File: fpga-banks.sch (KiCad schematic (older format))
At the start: 14 parts, among them U1 XC7K70T-FBG484, U2 ASEM1-100.000MHZ-LC-T

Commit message: Update caps around ADC
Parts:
- removed C2, C4: C_1n_0603, lpddr4-test-board-footprints:0603-cap, symbol lpddr4-test-board:C_1n_0603
- added C2, C4, C71: C_910p_0402, lpddr4-test-board-footprints:0402-res, symbol lpddr4-test-board:C_910p_0402
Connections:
- wire segments 207 -> 209
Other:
- moved on the sheet: C1
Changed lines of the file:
@@
 Wire Wire Line
 	8150 8700 9025 8700
-Wire Wire Line
-	9325 8700 9650 8700
 $Comp
 L lpddr4-test-board:R_100R_0402 R5
@@
 Wire Wire Line
 	8150 9000 9025 9000
-Wire Wire Line
-	9325 9000 9650 9000
 $Comp
 L lpddr4-test-board:R_100R_0402 R3
@@
 L lpddr4-test-board:C_910p_0402 C1
 U 1 1 6045F2AB
-P 9650 8850
-F 0 "C1" H 9675 8950 60  0000 L CNN
-F 1 "C_910p_0402" H 9650 8700 60  0001 C CNN
-F 2 "lpddr4-test-board-footprints:0402-res" H 9850 9050 60  0001 L CNN
-F 3 "" H 9650 8850 50  0001 C CNN
-F 4 "KEMET" H 9850 9250 60  0001 L CNN "Manufacturer"
-F 5 "C0402C911J5GACTU" H 9850 9150 60  0001 L CNN "MPN"
-F 6 "910p" H 9675 8750 50  0000 L CNN "Val"
-	1    9650 8850
-	1    0    0    -1
-$EndComp
-Wire Wire Line
-	9325 9250 9675 9250
-Wire Wire Line
-	9325 9550 9675 9550
-Wire Wire Line
-	9325 10300 9675 10300
-Wire Wire Line
-	9325 10600 9675 10600
-$Comp
-L lpddr4-test-board:C_1n_0603 C4
-U 1 1 604796AE
-P 9675 10450
-F 0 "C4" H 9700 10550 60  0000 L CNN
-F 1 "C_1n_0603" H 9675 10300 60  0001 C CNN
-F 2 "lpddr4-test-board-footprints:0603-cap" H 9875 10650 60  0001 L CNN
-F 3 "" H 9675 10450 50  0001 C CNN
-F 4 "AVX" H 9875 10850 60  0001 L CNN "Manufacturer"
-F 5 "06031C102JAT2A" H 9875 10750 60  0001 L CNN "MPN"
-F 6 "1n" H 9700 10350 50  0000 L CNN "Val"
-	1    9675 10450
-	1    0    0    -1
-$EndComp
-Connection ~ 9675 10300
-Wire Wire Line
-	9675 10300 10200 10300
-Connection ~ 9675 10600
-Wire Wire Line
-	9675 10600 10200 10600
-$Comp
-L lpddr4-test-board:C_1n_0603 C2
-U 1 1 6049AB42
-P 9675 9400
-F 0 "C2" H 9700 9500 60  0000 L CNN
-F 1 "C_1n_0603" H 9675 9250 60  0001 C CNN
-F 2 "lpddr4-test-board-footprints:0603-cap" H 9875 9600 60  0001 L CNN
-F 3 "" H 9675 9400 50  0001 C CNN
-F 4 "AVX" H 9875 9800 60  0001 L CNN "Manufacturer"
-F 5 "06031C102JAT2A" H 9875 9700 60  0001 L CNN "MPN"
-F 6 "1n" H 9700 9300 50  0000 L CNN "Val"
-	1    9675 9400
-	1    0    0    -1
-$EndComp
-Connection ~ 9675 9250
-Wire Wire Line
-	9675 9250 10200 9250
-Connection ~ 9675 9550
-Wire Wire Line
-	9675 9550 10200 9550
-Connection ~ 9650 8700
-Wire Wire Line
-	9650 8700 10200 8700
-Connection ~ 9650 9000
-Wire Wire Line
-	9650 9000 10200 9000
+P 9700 8850
+F 0 "C1" H 9725 8950 60  0000 L CNN
+F 1 "C_910p_0402" H 9700 8700 60  0001 C CNN
+F 2 "lpddr4-test-board-footprints:0402-res" H 9900 9050 60  0001 L CNN
+F 3 "" H 9700 8850 50  0001 C CNN
+F 4 "KEMET" H 9900 9250 60  0001 L CNN "Manufacturer"
+F 5 "C0402C911J5GACTU" H 9900 9150 60  0001 L CNN "MPN"
+F 6 "910p" H 9725 8750 50  0000 L CNN "Val"
+	1    9700 8850
+	1    0    0    -1
+$EndComp
 Text GLabel 5150 7000 2    50   Input ~ 0
 TMDS_CLK_P
@@
 Connection ~ 8225 1350
 Wire Wire Line
-	9325 9750 10200 9750
-Wire Wire Line
-	9325 10050 10200 10050
+	9325 9750 9700 9750
+Wire Wire Line
+	9325 10050 9700 10050
 Text GLabel 7075 7750 0    50   Input ~ 0
 ETH_REF_CLK
@@
 Text GLabel 10525 4075 2    50   Input ~ 0
 USR_BTN4
+$Comp
+L lpddr4-test-board:C_910p_0402 C4
+U 1 1 5FC5316D
+P 9700 9900
+F 0 "C4" H 9725 10000 60  0000 L CNN
+F 1 "C_910p_0402" H 9700 9750 60  0001 C CNN
+F 2 "lpddr4-test-board-footprints:0402-res" H 9900 10100 60  0001 L CNN
+F 3 "" H 9700 9900 50  0001 C CNN
+F 4 "KEMET" H 9900 10300 60  0001 L CNN "Manufacturer"
+F 5 "C0402C911J5GACTU" H 9900 10200 60  0001 L CNN "MPN"
+F 6 "910p" H 9725 9800 50  0000 L CNN "Val"
+	1    9700 9900
+	1    0    0    -1
+$EndComp
+Connection ~ 9700 9750
+Wire Wire Line
+	9700 9750 10200 9750
+Connection ~ 9700 10050
+Wire Wire Line
+	9700 10050 10200 10050
+Wire Wire Line
+	9325 9250 9700 9250
+Wire Wire Line
+	9325 9550 9700 9550
+Wire Wire Line
+	9325 10300 9700 10300
+Wire Wire Line
+	9325 10600 9700 10600
+$Comp
+L lpddr4-test-board:C_910p_0402 C71
+U 1 1 5FC539B0
+P 9700 10450
+F 0 "C71" H 9725 10550 60  0000 L CNN
+F 1 "C_910p_0402" H 9700 10300 60  0001 C CNN
+F 2 "lpddr4-test-board-footprints:0402-res" H 9900 10650 60  0001 L CNN
+F 3 "" H 9700 10450 50  0001 C CNN
+F 4 "KEMET" H 9900 10850 60  0001 L CNN "Manufacturer"
+F 5 "C0402C911J5GACTU" H 9900 10750 60  0001 L CNN "MPN"
+F 6 "910p" H 9725 10350 50  0000 L CNN "Val"
+	1    9700 10450
+	1    0    0    -1
+$EndComp
+Connection ~ 9700 10300
+Wire Wire Line
+	9700 10300 10200 10300
+Connection ~ 9700 10600
+Wire Wire Line
+	9700 10600 10200 10600
+$Comp
+L lpddr4-test-board:C_910p_0402 C2
+U 1 1 5FC53CE5
+P 9700 9400
+F 0 "C2" H 9725 9500 60  0000 L CNN
+F 1 "C_910p_0402" H 9700 9250 60  0001 C CNN
+F 2 "lpddr4-test-board-footprints:0402-res" H 9900 9600 60  0001 L CNN
+F 3 "" H 9700 9400 50  0001 C CNN
+F 4 "KEMET" H 9900 9800 60  0001 L CNN "Manufacturer"
+F 5 "C0402C911J5GACTU" H 9900 9700 60  0001 L CNN "MPN"
+F 6 "910p" H 9725 9300 50  0000 L CNN "Val"
+	1    9700 9400
+	1    0    0    -1
+$EndComp
+Connection ~ 9700 9250
+Wire Wire Line
+	9700 9250 10200 9250
+Connection ~ 9700 9550
+Wire Wire Line
+	9700 9550 10200 9550
+Connection ~ 9700 8700
+Wire Wire Line
+	9700 8700 10200 8700
+Connection ~ 9700 9000
+Wire Wire Line
+	9700 9000 10200 9000
+Wire Wire Line
+	9325 9000 9700 9000
+Wire Wire Line
+	9325 8700 9700 8700
 $EndSCHEMATC

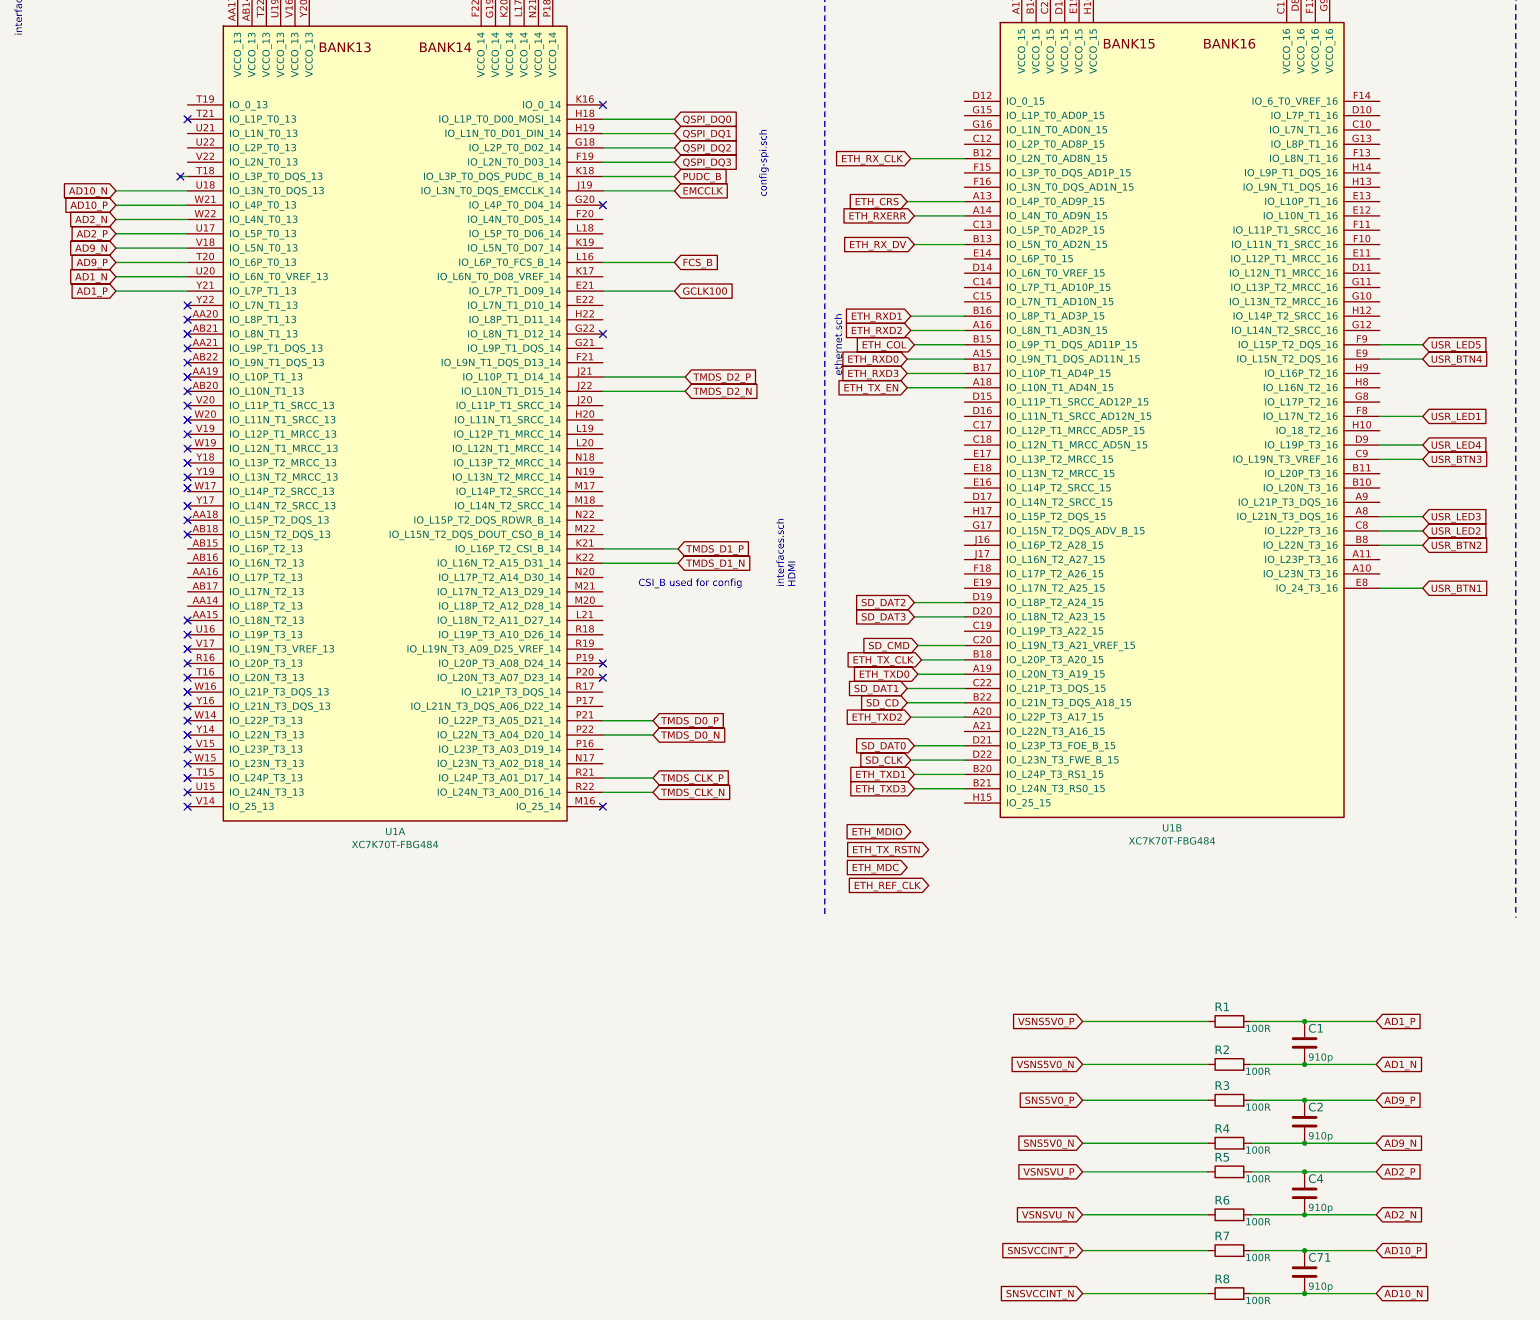
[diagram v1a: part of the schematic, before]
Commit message: Remove unused ADC channels
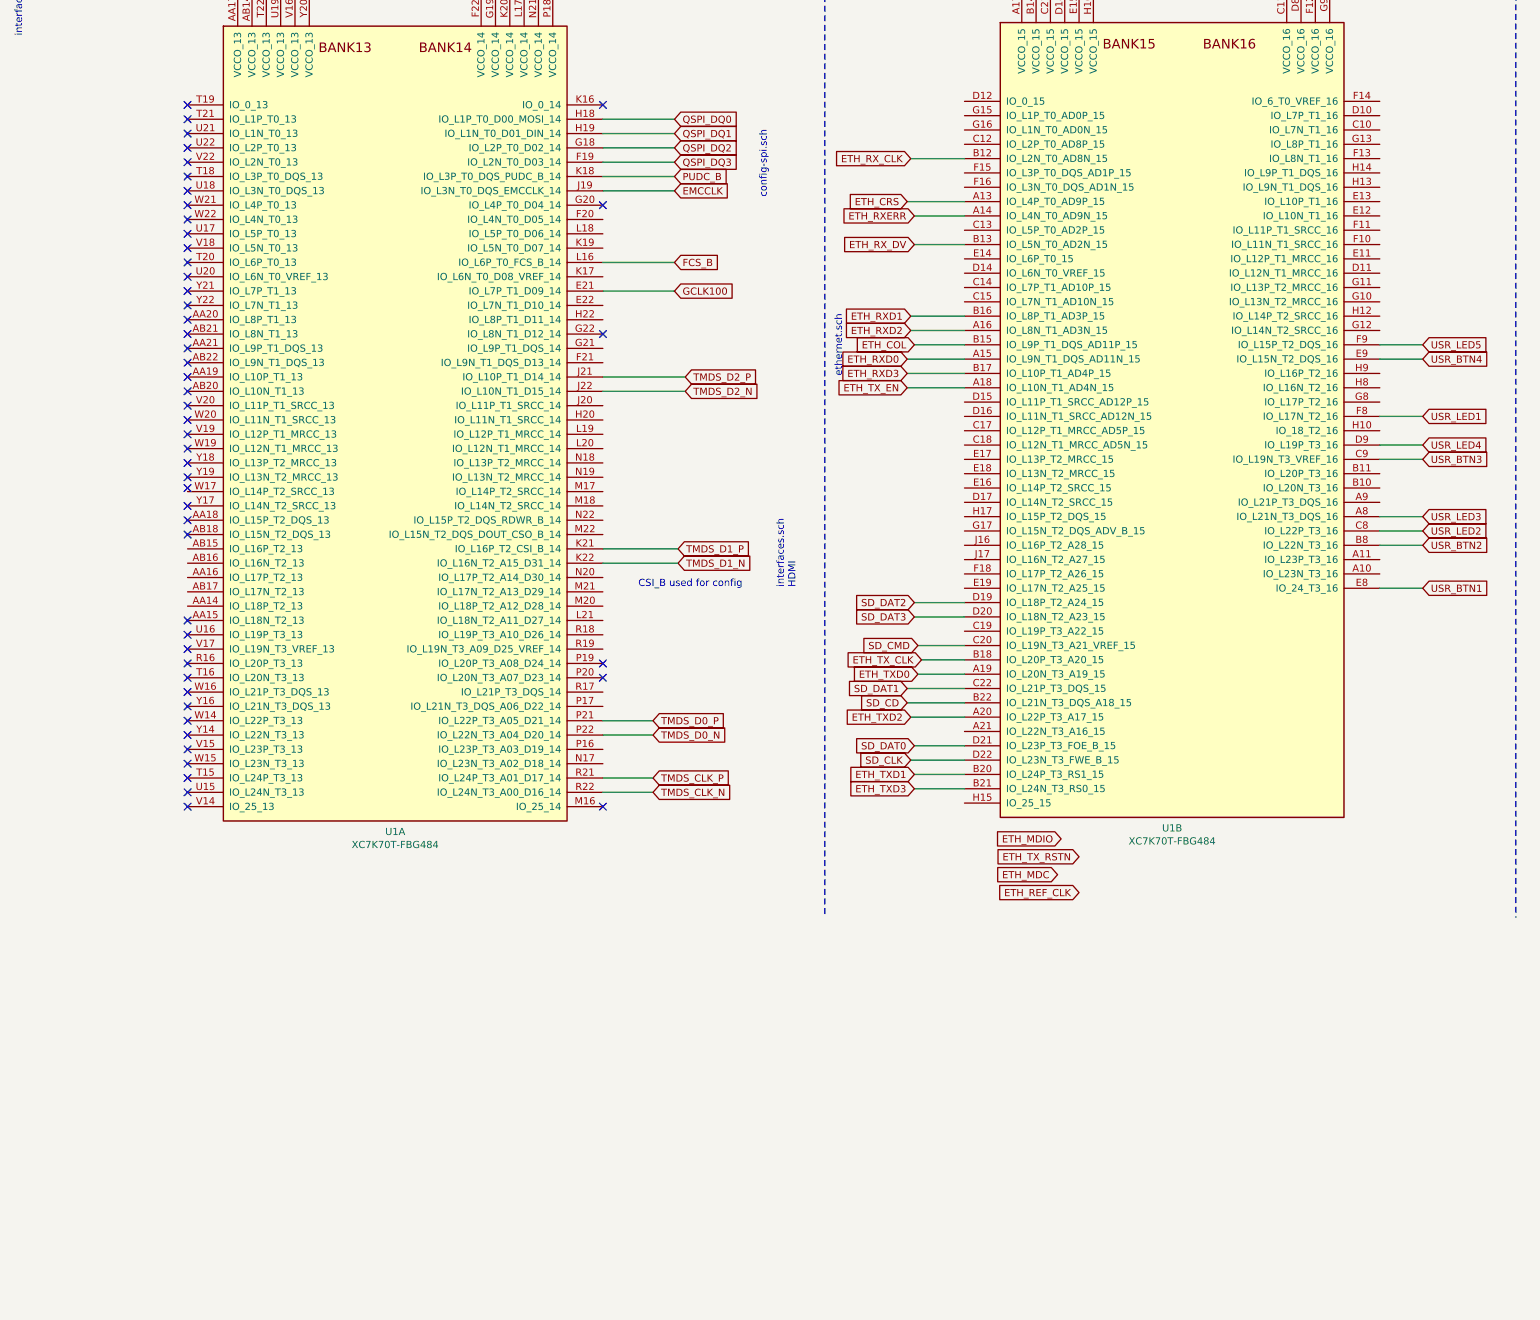
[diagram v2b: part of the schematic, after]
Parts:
- removed C1, C2, C4, C71: C_910p_0402, lpddr4-test-board-footprints:0402-res, symbol lpddr4-test-board:C_910p_0402
- removed R1, R2, R3, R4, R5, R6, R7, R8: R_100R_0402, lpddr4-test-board-footprints:0402-res, symbol lpddr4-test-board:R_100R_0402
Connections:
- net AD10_N: no longer names the net of U1.U18 (IO_L3N_T0_DQS_13)
- net AD10_P: no longer names the net of U1.W21 (IO_L4P_T0_13)
- net AD1_N: no longer names the net of U1.U20 (IO_L6N_T0_VREF_13)
- net AD1_P: no longer names the net of U1.Y21 (IO_L7P_T1_13)
- net AD2_N: no longer names the net of U1.W22 (IO_L4N_T0_13)
- net AD2_P: no longer names the net of U1.U17 (IO_L5P_T0_13)
- net AD9_N: no longer names the net of U1.V18 (IO_L5N_T0_13)
- net AD9_P: no longer names the net of U1.T20 (IO_L6P_T0_13)
- no-connect marks 45 -> 57

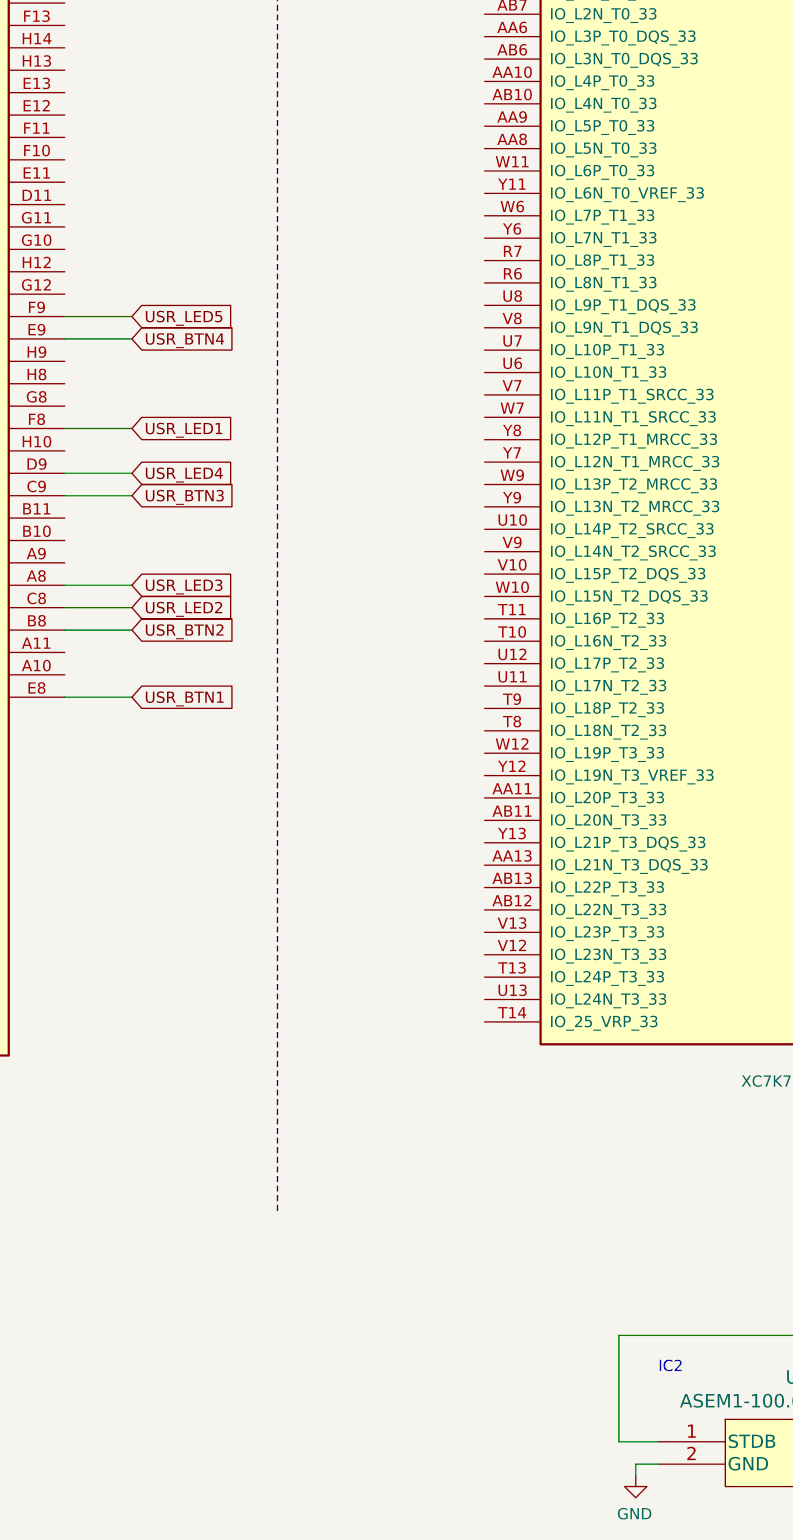
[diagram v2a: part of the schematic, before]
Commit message: Reconnect FTDI UART lanes
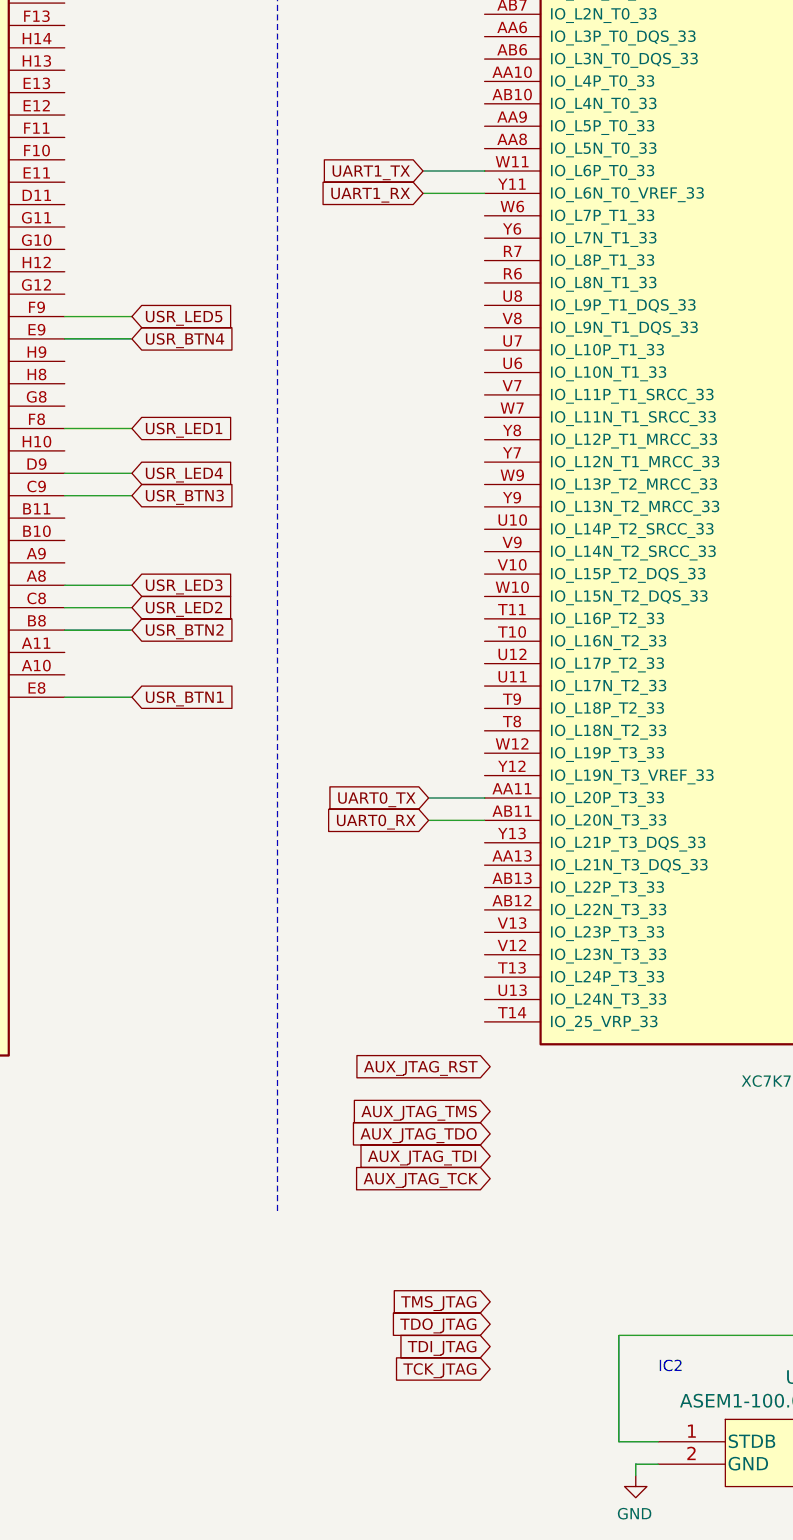
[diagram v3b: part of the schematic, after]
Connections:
- net UART0_TX: now reaches U1.AA11 (IO_L20P_T3_33)
- net UART0_RX: now reaches U1.AB11 (IO_L20N_T3_33)
- net UART1_TX: now reaches U1.W11 (IO_L6P_T0_33)
- net UART1_RX: now reaches U1.Y11 (IO_L6N_T0_VREF_33)
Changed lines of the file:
@@
 $EndComp
 NoConn ~ 1900 2800
+Text GLabel 12125 8675 0    50   Input ~ 0
+TCK_JTAG
+Text GLabel 12125 8575 0    50   Input ~ 0
+TDI_JTAG
+Text GLabel 12125 8475 0    50   Input ~ 0
+TDO_JTAG
+Text GLabel 12125 8375 0    50   Input ~ 0
+TMS_JTAG
+Text GLabel 12125 7725 0    50   Input ~ 0
+AUX_JTAG_TDI
+Text GLabel 12125 7625 0    50   Input ~ 0
+AUX_JTAG_TDO
+Text GLabel 12125 7525 0    50   Input ~ 0
+AUX_JTAG_TMS
+Text GLabel 11850 6225 0    50   Input ~ 0
+UART0_RX
+Text GLabel 11825 3425 0    50   Input ~ 0
+UART1_RX
+Text GLabel 11850 6125 0    50   Input ~ 0
+UART0_TX
+Text GLabel 11825 3325 0    50   Input ~ 0
+UART1_TX
+Text GLabel 12125 7825 0    50   Input ~ 0
+AUX_JTAG_TCK
+Text GLabel 12125 7325 0    50   Input ~ 0
+AUX_JTAG_RST
+Wire Wire Line
+	12100 6225 11850 6225
+Wire Wire Line
+	12100 6125 11850 6125
+Wire Wire Line
+	12100 3325 11825 3325
+Wire Wire Line
+	12100 3425 11825 3425
 $EndSCHEMATC
